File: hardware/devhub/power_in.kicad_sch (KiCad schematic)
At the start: 24 parts, among them J1 USB-C PWR IN, U1 AP7361C-33E, U13 TPS259470ARPWR

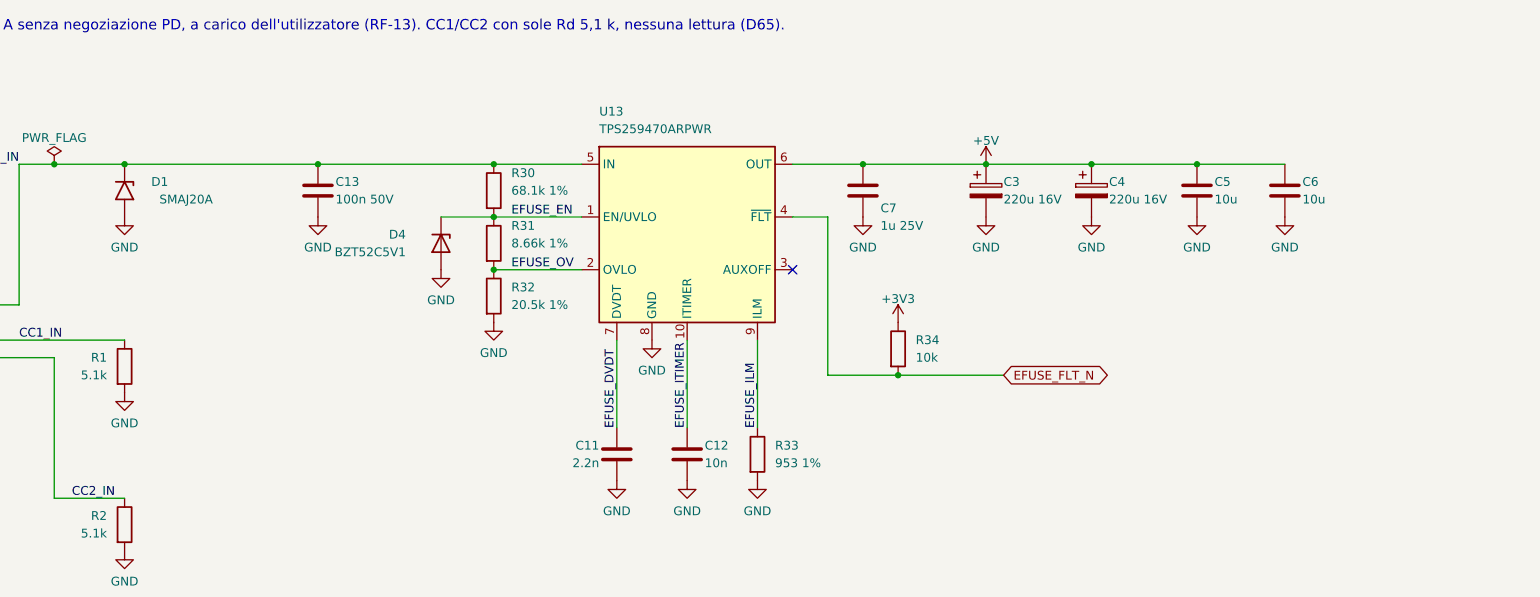
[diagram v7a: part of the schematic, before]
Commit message: Restore relay LED, larger NC/NO jumper, PCB routing progress (D89, D90)
- D90/R90 relay LED back on RLY1, in the front LED row in line with SW1;
  host LED D93/R93 moved to the rear next to J1
- JP2: project footprint with 2.0x3.0 mm pads, 2.4 mm pitch and 1.0 mm
  bridge for 3 A relay contacts
- U13: 0.2 mm tracks from pads 8/9 alongside the corner pads, no clearance
  exception
- Routing and placement progress, zone defaults, schematic layout cleanup
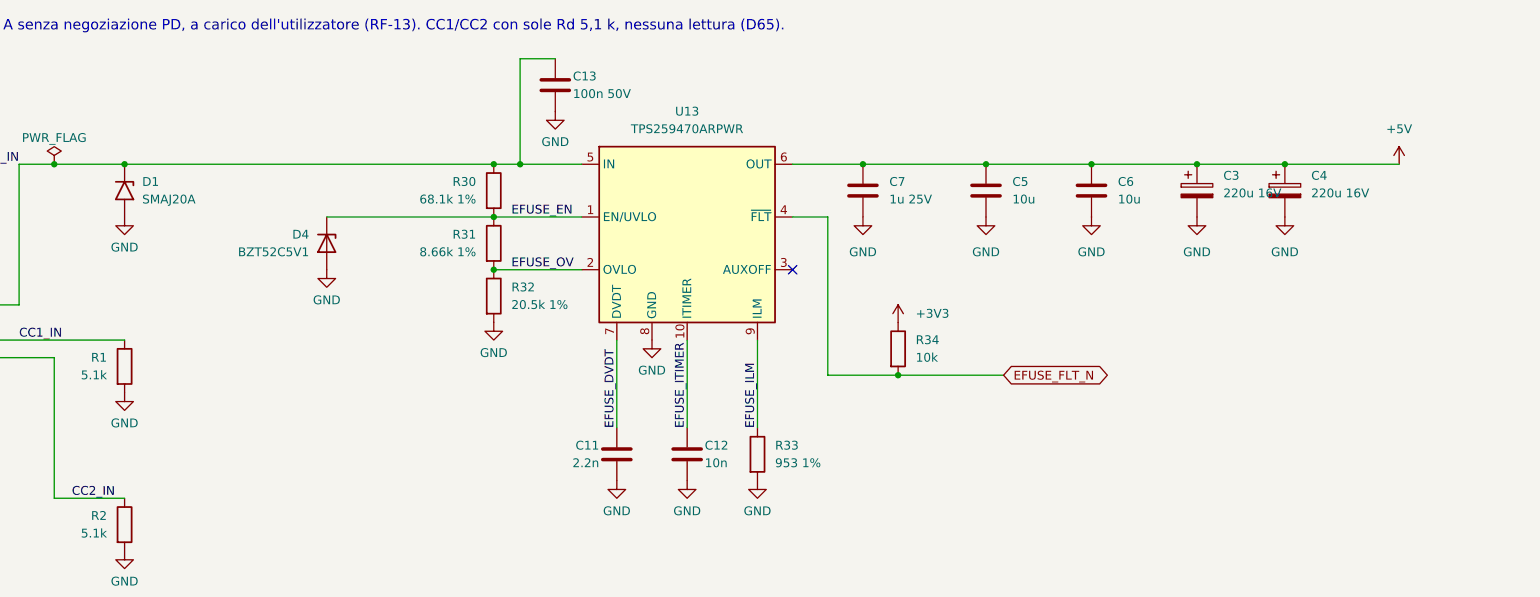
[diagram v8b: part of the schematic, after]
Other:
- moved on the sheet: C13, C3, C4, C5, C6, D4
